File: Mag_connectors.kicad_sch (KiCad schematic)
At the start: 3 parts

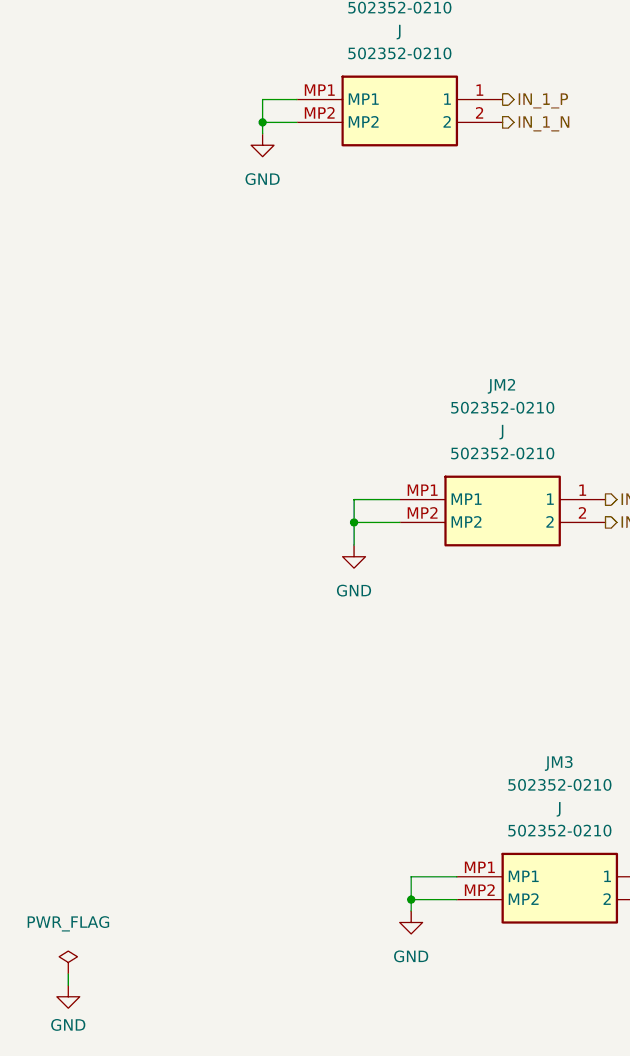
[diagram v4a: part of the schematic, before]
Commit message: Max ERC errors corrected
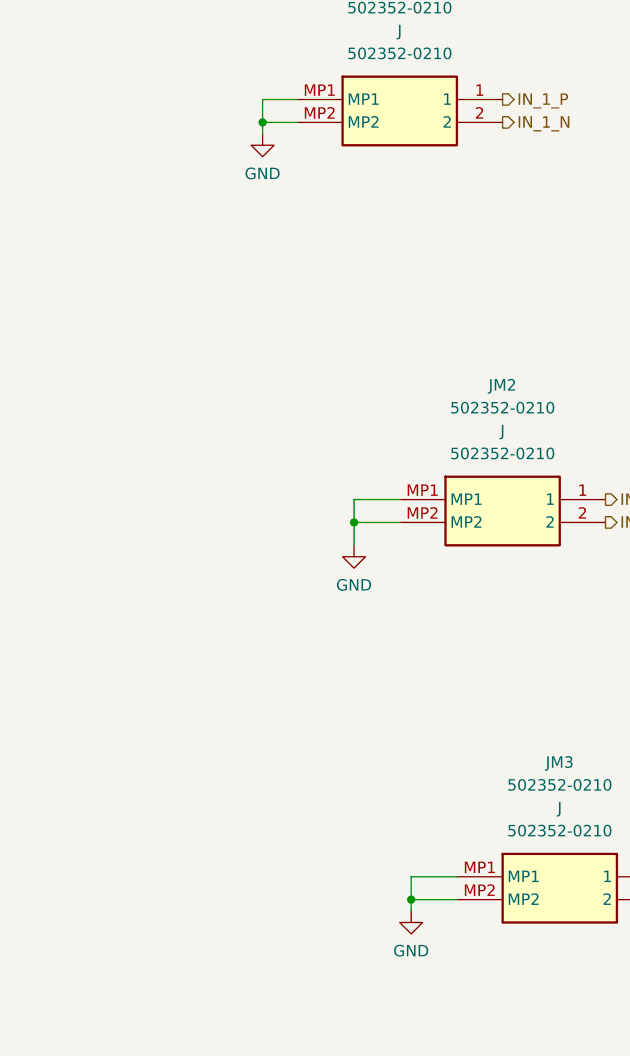
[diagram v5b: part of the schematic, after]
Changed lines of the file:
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@@
-    (stroke (width 0) (type default) (color 0 0 0 0))
-  )
-  (wire (pts (xy 39.37 147.955) (xy 39.37 146.685))
     (stroke (width 0) (type default) (color 0 0 0 0))
   )
@@
     (effects (font (size 1.27 1.27)) (justify left))
   )
-  (symbol (lib_id "power:GND") (at 60.96 53.34 0) (unit 1)
-    (in_bom yes) (on_board yes) (fields_autoplaced)
-    (property "Reference" "#PWR0250" (id 0) (at 60.96 59.69 0)
-      (effects (font (size 1.27 1.27)) hide)
-    )
-    (property "Value" "GND" (id 1) (at 60.96 58.42 0))
-    (property "Footprint" "" (id 2) (at 60.96 53.34 0)
-      (effects (font (size 1.27 1.27)) hide)
-    )
-    (property "Datasheet" "" (id 3) (at 60.96 53.34 0)
-      (effects (font (size 1.27 1.27)) hide)
-    )
-    (pin "1")
-  )
-  (symbol (lib_id "power:GND") (at 77.47 139.7 0) (unit 1)
-    (in_bom yes) (on_board yes) (fields_autoplaced)
-    (property "Reference" "#PWR0252" (id 0) (at 77.47 146.05 0)
-      (effects (font (size 1.27 1.27)) hide)
-    )
-    (property "Value" "GND" (id 1) (at 77.47 144.78 0))
-    (property "Footprint" "" (id 2) (at 77.47 139.7 0)
-      (effects (font (size 1.27 1.27)) hide)
-    )
-    (property "Datasheet" "" (id 3) (at 77.47 139.7 0)
-      (effects (font (size 1.27 1.27)) hide)
-    )
-    (pin "1")
-  )
   (symbol (lib_id "502352-0210:502352-0210") (at 64.77 49.53 0) (unit 1)
     (in_bom yes) (on_board yes) (fields_autoplaced)
@@
     (pin "MP1")
     (pin "MP2")
-  )
-  (symbol (lib_id "power:GND") (at 39.37 147.955 0) (unit 1)
-    (in_bom yes) (on_board yes) (fields_autoplaced)
-    (property "Reference" "#PWR0279" (id 0) (at 39.37 154.305 0)
-      (effects (font (size 1.27 1.27)) hide)
-    )
-    (property "Value" "GND" (id 1) (at 39.37 152.4 0))
-    (property "Footprint" "" (id 2) (at 39.37 147.955 0)
-      (effects (font (size 1.27 1.27)) hide)
-    )
-    (property "Datasheet" "" (id 3) (at 39.37 147.955 0)
-      (effects (font (size 1.27 1.27)) hide)
-    )
-    (pin "1")
   )
   (symbol (lib_id "502352-0210:502352-0210") (at 82.55 135.89 0) (unit 1)
@@
     (pin "MP2")
   )
-  (symbol (lib_id "power:GND") (at 71.12 99.06 0) (unit 1)
+  (symbol (lib_id "upsat-comms-hardware:GND") (at 60.96 53.34 0) (unit 1)
     (in_bom yes) (on_board yes) (fields_autoplaced)
-    (property "Reference" "#PWR0251" (id 0) (at 71.12 105.41 0)
+    (property "Reference" "#PWR0235" (id 0) (at 60.96 59.69 0)
       (effects (font (size 1.27 1.27)) hide)
     )
-    (property "Value" "GND" (id 1) (at 71.12 104.14 0))
-    (property "Footprint" "" (id 2) (at 71.12 99.06 0)
+    (property "Value" "GND" (id 1) (at 60.96 57.785 0))
+    (property "Footprint" "" (id 2) (at 60.96 53.34 0))
+    (property "Datasheet" "" (id 3) (at 60.96 53.34 0))
+    (pin "1")
+  )
+  (symbol (lib_id "upsat-comms-hardware:GND") (at 77.47 139.7 0) (unit 1)
+    (in_bom yes) (on_board yes) (fields_autoplaced)
+    (property "Reference" "#PWR0245" (id 0) (at 77.47 146.05 0)
       (effects (font (size 1.27 1.27)) hide)
     )
-    (property "Datasheet" "" (id 3) (at 71.12 99.06 0)
+    (property "Value" "GND" (id 1) (at 77.47 144.145 0))
+    (property "Footprint" "" (id 2) (at 77.47 139.7 0))
+    (property "Datasheet" "" (id 3) (at 77.47 139.7 0))
+    (pin "1")
+  )
+  (symbol (lib_id "upsat-comms-hardware:GND") (at 71.12 99.06 0) (unit 1)
+    (in_bom yes) (on_board yes) (fields_autoplaced)
+    (property "Reference" "#PWR0246" (id 0) (at 71.12 105.41 0)
       (effects (font (size 1.27 1.27)) hide)
     )
+    (property "Value" "GND" (id 1) (at 71.12 103.505 0))
+    (property "Footprint" "" (id 2) (at 71.12 99.06 0))
+    (property "Datasheet" "" (id 3) (at 71.12 99.06 0))
     (pin "1")
   )
-  (symbol (lib_id "power:PWR_FLAG") (at 39.37 146.685 0) (unit 1)
-    (in_bom yes) (on_board yes) (fields_autoplaced)
-    (property "Reference" "#FLG0115" (id 0) (at 39.37 144.78 0)
-      (effects (font (size 1.27 1.27)) hide)
-    )
-    (property "Value" "PWR_FLAG" (id 1) (at 39.37 140.97 0))
-    (property "Footprint" "" (id 2) (at 39.37 146.685 0)
-      (effects (font (size 1.27 1.27)) hide)
-    )
-    (property "Datasheet" "~" (id 3) (at 39.37 146.685 0)
-      (effects (font (size 1.27 1.27)) hide)
-    )
-    (pin "1")
-  )

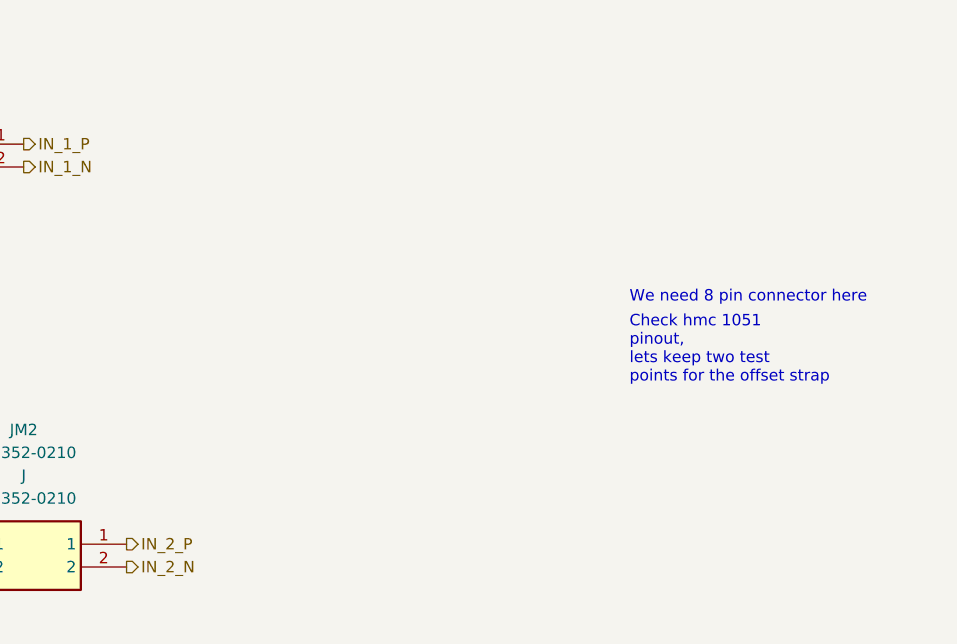
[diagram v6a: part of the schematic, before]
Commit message: Updated 8 pin connector for magentometer
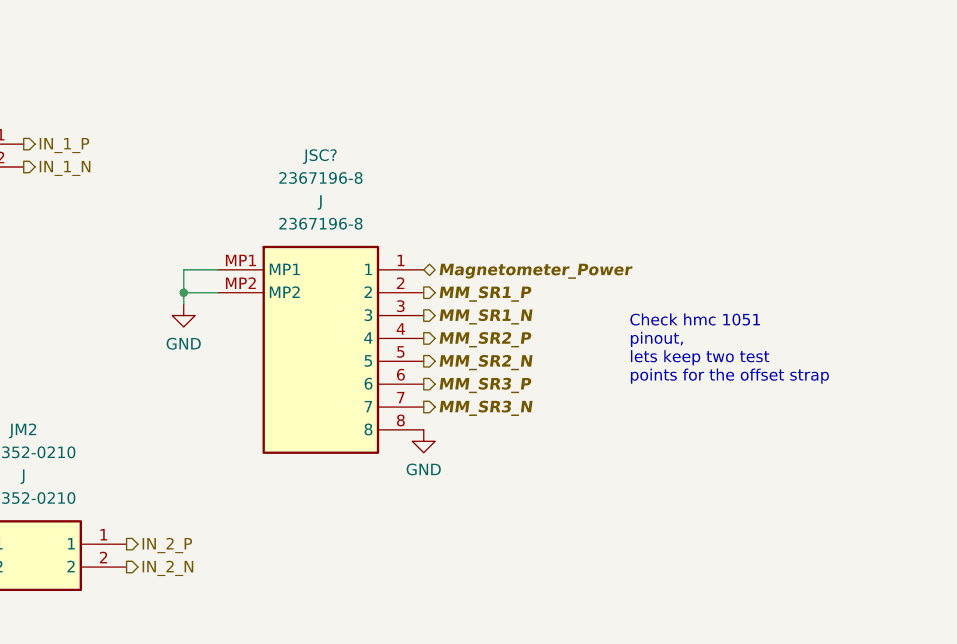
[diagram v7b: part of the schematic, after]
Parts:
- added JSC?: 2367196-8, symbol 2367196-8:2367196-8
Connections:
- net GND: now also JSC?.8, JSC?.MP1, JSC?.MP2
- new net MM_SR1_N: JSC?.3
- new net MM_SR1_P: JSC?.2
- new net MM_SR2_N: JSC?.5
- new net MM_SR2_P: JSC?.4
- new net MM_SR3_N: JSC?.7
- new net MM_SR3_P: JSC?.6
- new net Magnetometer_Power: JSC?.1
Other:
- note removed: "We need 8 pin connector here"
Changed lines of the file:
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@@
   (junction (at 71.12 96.52) (diameter 0) (color 0 0 0 0)
   )
+  (junction (at 105.41 66.04) (diameter 0) (color 0 0 0 0)
+  )
   (junction (at 60.96 52.07) (diameter 0) (color 0 0 0 0)
   )
@@
     (stroke (width 0) (type default) (color 0 0 0 0))
   )
+  (wire (pts (xy 105.41 63.5) (xy 105.41 66.04))
+    (stroke (width 0) (type default) (color 0 0 0 0))
+  )
   (wire (pts (xy 60.96 49.53) (xy 60.96 52.07))
     (stroke (width 0) (type default) (color 0 0 0 0))
@@
     (stroke (width 0) (type default) (color 0 0 0 0))
   )
+  (wire (pts (xy 105.41 66.04) (xy 109.22 66.04))
+    (stroke (width 0) (type default) (color 0 0 0 0))
+  )
   (wire (pts (xy 60.96 52.07) (xy 60.96 53.34))
+    (stroke (width 0) (type default) (color 0 0 0 0))
+  )
+  (wire (pts (xy 105.41 66.04) (xy 105.41 67.31))
+    (stroke (width 0) (type default) (color 0 0 0 0))
+  )
+  (wire (pts (xy 109.22 63.5) (xy 105.41 63.5))
     (stroke (width 0) (type default) (color 0 0 0 0))
   )
@@
     (effects (font (size 1.27 1.27)) (justify left bottom))
   )
-  (text "We need 8 pin connector here \n" (at 154.94 67.31 0)
-    (effects (font (size 1.27 1.27)) (justify left bottom))
+  (hierarchical_label "MM_SR3_P" (shape output) (at 132.08 76.2 0)
+    (effects (font (size 1.27 1.27) bold italic) (justify left))
   )
   (hierarchical_label "IN_3_P" (shape output) (at 105.41 135.89 0)
     (effects (font (size 1.27 1.27)) (justify left))
   )
+  (hierarchical_label "MM_SR2_N" (shape output) (at 132.08 73.66 0)
+    (effects (font (size 1.27 1.27) bold italic) (justify left))
+  )
   (hierarchical_label "IN_1_N" (shape output) (at 87.63 52.07 0)
     (effects (font (size 1.27 1.27)) (justify left))
@@
     (effects (font (size 1.27 1.27)) (justify left))
   )
+  (hierarchical_label "MM_SR1_N" (shape output) (at 132.08 68.58 0)
+    (effects (font (size 1.27 1.27) bold italic) (justify left))
+  )
+  (hierarchical_label "MM_SR2_P" (shape output) (at 132.08 71.12 0)
+    (effects (font (size 1.27 1.27) bold italic) (justify left))
+  )
   (hierarchical_label "IN_2_P" (shape output) (at 99.06 93.98 0)
     (effects (font (size 1.27 1.27)) (justify left))
+  )
+  (hierarchical_label "MM_SR3_N" (shape output) (at 132.08 78.74 0)
+    (effects (font (size 1.27 1.27) bold italic) (justify left))
+  )
+  (hierarchical_label "MM_SR1_P" (shape output) (at 132.08 66.04 0)
+    (effects (font (size 1.27 1.27) bold italic) (justify left))
+  )
+  (hierarchical_label "Magnetometer_Power" (shape bidirectional) (at 132.08 63.5 0)
+    (effects (font (size 1.27 1.27) bold italic) (justify left))
   )
   (hierarchical_label "IN_3_N" (shape output) (at 105.41 138.43 0)
@@
     (pin "MP2")
   )
+  (symbol (lib_id "upsat-comms-hardware:GND") (at 105.41 67.31 0) (unit 1)
+    (in_bom yes) (on_board yes) (fields_autoplaced)
+    (property "Reference" "#PWR?" (id 0) (at 105.41 73.66 0)
+      (effects (font (size 1.27 1.27)) hide)
+    )
+    (property "Value" "GND" (id 1) (at 105.41 71.755 0))
+    (property "Footprint" "" (id 2) (at 105.41 67.31 0))
+    (property "Datasheet" "" (id 3) (at 105.41 67.31 0))
+    (pin "1")
+  )
+  (symbol (lib_id "2367196-8:2367196-8") (at 109.22 63.5 0) (unit 1)
+    (in_bom yes) (on_board yes) (fields_autoplaced)
+    (property "Reference" "JSC?" (id 0) (at 120.65 50.8 0))
+    (property "Value" "2367196-8" (id 1) (at 120.65 53.34 0))
+    (property "Footprint" "" (id 2) (at 109.22 63.5 0)
+      (effects (font (size 1.27 1.27)) hide)
+    )
+    (property "Datasheet" "" (id 3) (at 109.22 63.5 0)
+      (effects (font (size 1.27 1.27)) hide)
+    )
+    (property "Reference_1" "J" (id 4) (at 120.65 55.88 0))
+    (property "Value_1" "2367196-8" (id 5) (at 120.65 58.42 0))
+    (property "Footprint_1" "23671968" (id 6) (at 128.27 158.42 0)
+      (effects (font (size 1.27 1.27)) (justify left top) hide)
+    )
+    (property "Datasheet_1" "https://www.te.com/commerce/DocumentDelivery/DDEController?Action=showdoc&DocId=Customer+Drawing%7F2367196%7FA%7Fpdf%7FEnglish%7FENG_CD_2367196_A.pdf%7F2367196-8" (id 7) (at 128.27 258.42 0)
+      (effects (font (size 1.27 1.27)) (justify left top) hide)
+    )
+    (property "Height" "3.25" (id 8) (at 128.27 458.42 0)
+      (effects (font (size 1.27 1.27)) (justify left top) hide)
+    )
+    (property "Mouser Part Number" "571-2367196-8" (id 9) (at 128.27 558.42 0)
+      (effects (font (size 1.27 1.27)) (justify left top) hide)
+    )
+    (property "Mouser Price/Stock" "https://www.mouser.co.uk/ProductDetail/TE-Connectivity/2367196-8?qs=sPbYRqrBIVndDqCjm2TjhA%3D%3D" (id 10) (at 128.27 658.42 0)
+      (effects (font (size 1.27 1.27)) (justify left top) hide)
+    )
+    (property "Manufacturer_Name" "TE Connectivity" (id 11) (at 128.27 758.42 0)
+      (effects (font (size 1.27 1.27)) (justify left top) hide)
+    )
+    (property "Manufacturer_Part_Number" "2367196-8" (id 12) (at 128.27 858.42 0)
+      (effects (font (size 1.27 1.27)) (justify left top) hide)
+    )
+    (pin "1")
+    (pin "2")
+    (pin "3")
+    (pin "4")
+    (pin "5")
+    (pin "6")
+    (pin "7")
+    (pin "8")
+    (pin "MP1")
+    (pin "MP2")
+  )
   (symbol (lib_id "upsat-comms-hardware:GND") (at 60.96 53.34 0) (unit 1)
     (in_bom yes) (on_board yes) (fields_autoplaced)
@@
     (pin "1")
   )
+  (symbol (lib_id "upsat-comms-hardware:GND") (at 132.08 81.28 0) (unit 1)
+    (in_bom yes) (on_board yes) (fields_autoplaced)
+    (property "Reference" "#PWR?" (id 0) (at 132.08 87.63 0)
+      (effects (font (size 1.27 1.27)) hide)
+    )
+    (property "Value" "GND" (id 1) (at 132.08 85.725 0))
+    (property "Footprint" "" (id 2) (at 132.08 81.28 0))
+    (property "Datasheet" "" (id 3) (at 132.08 81.28 0))
+    (pin "1")
+  )

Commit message: Updated the changes
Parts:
- gave numbers to parts that had none: 1
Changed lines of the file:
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@@
   (symbol (lib_id "upsat-comms-hardware:GND") (at 105.41 67.31 0) (unit 1)
     (in_bom yes) (on_board yes) (fields_autoplaced)
-    (property "Reference" "#PWR?" (id 0) (at 105.41 73.66 0)
+    (property "Reference" "#PWR0151" (id 0) (at 105.41 73.66 0)
       (effects (font (size 1.27 1.27)) hide)
     )
@@
   (symbol (lib_id "2367196-8:2367196-8") (at 109.22 63.5 0) (unit 1)
     (in_bom yes) (on_board yes) (fields_autoplaced)
-    (property "Reference" "JSC?" (id 0) (at 120.65 50.8 0))
+    (property "Reference" "JSC1" (id 0) (at 120.65 50.8 0))
     (property "Value" "2367196-8" (id 1) (at 120.65 53.34 0))
     (property "Footprint" "" (id 2) (at 109.22 63.5 0)
@@
   (symbol (lib_id "upsat-comms-hardware:GND") (at 60.96 53.34 0) (unit 1)
     (in_bom yes) (on_board yes) (fields_autoplaced)
-    (property "Reference" "#PWR0235" (id 0) (at 60.96 59.69 0)
+    (property "Reference" "#PWR0150" (id 0) (at 60.96 59.69 0)
       (effects (font (size 1.27 1.27)) hide)
     )
@@
   (symbol (lib_id "upsat-comms-hardware:GND") (at 77.47 139.7 0) (unit 1)
     (in_bom yes) (on_board yes) (fields_autoplaced)
-    (property "Reference" "#PWR0245" (id 0) (at 77.47 146.05 0)
+    (property "Reference" "#PWR0154" (id 0) (at 77.47 146.05 0)
       (effects (font (size 1.27 1.27)) hide)
     )
@@
   (symbol (lib_id "upsat-comms-hardware:GND") (at 71.12 99.06 0) (unit 1)
     (in_bom yes) (on_board yes) (fields_autoplaced)
-    (property "Reference" "#PWR0246" (id 0) (at 71.12 105.41 0)
+    (property "Reference" "#PWR0153" (id 0) (at 71.12 105.41 0)
       (effects (font (size 1.27 1.27)) hide)
     )
@@
   (symbol (lib_id "upsat-comms-hardware:GND") (at 132.08 81.28 0) (unit 1)
     (in_bom yes) (on_board yes) (fields_autoplaced)
-    (property "Reference" "#PWR?" (id 0) (at 132.08 87.63 0)
+    (property "Reference" "#PWR0152" (id 0) (at 132.08 87.63 0)
       (effects (font (size 1.27 1.27)) hide)
     )
